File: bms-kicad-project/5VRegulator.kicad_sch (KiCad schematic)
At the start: 22 parts, among them U5 SIC461ED-T1-GE3

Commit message: feat: Forgot to save changes to schematic.
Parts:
- removed C37: 4.7u, FixedWing:CAPC2012X145N, symbol FixedWing:GCM21BC71E475KE36L
- removed R?: 3.3, FixedWing:RESC1608X55N, symbol FixedWing:RK73H1JTTD3R30F
- added R4, R?: 100k, FixedWing:RESC2012X60N, symbol FixedWing:RC0805FR-07100KL
- added R5: 3.3, FixedWing:RESC1608X55N, symbol FixedWing:RK73H1JTTD3R30F
- renumbered C38 to C?, C35 to C?, C36 to C?, U5 to U?
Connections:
- net +BATT: now also C?.2; no longer C?.N
- net GND: now also C?.1; no longer C?.2, C?.2, C?.P, R?.1, R?.1, R?.1, R?.2, R?.2
- net at R?.1, U?.3 (EN): now also R?.2; no longer R?.2
- net at U?.5 (PHASE), U?.6 (PHASE__1): now also C32.2
- net at C32.1: now also R5.2
- net at R?.1: no longer U?.24 (FSW)
- net at U?.4 (BOOT): now also R5.1; no longer C32.2
- new net: R4.1, R?.2
- new net: R4.2, R?.1
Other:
- moved on the sheet: R?

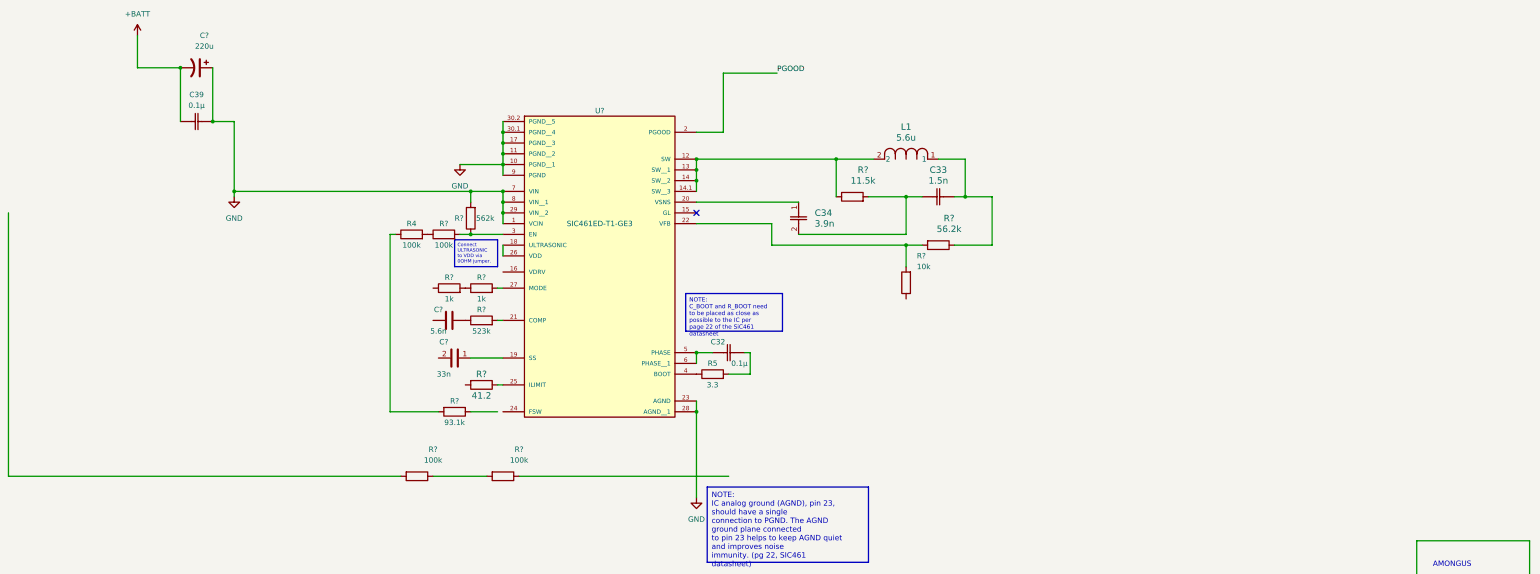
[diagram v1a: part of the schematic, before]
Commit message: feat: Just about completed 5V Regulator Schematic.
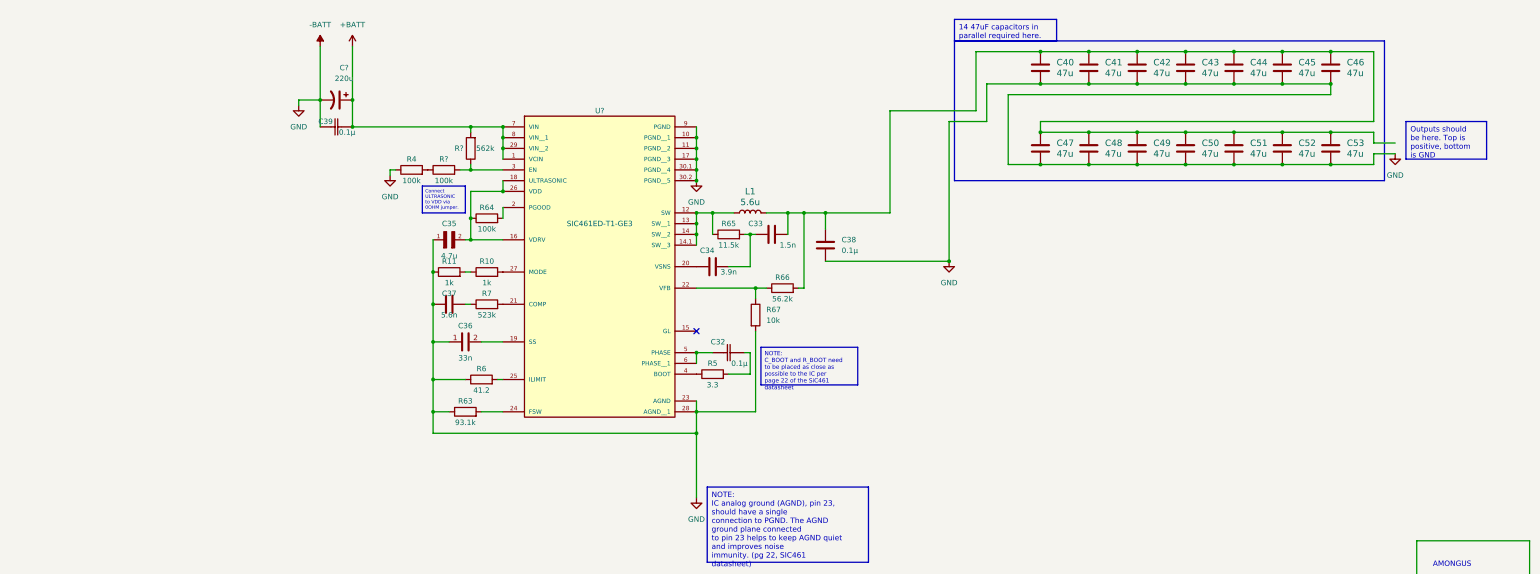
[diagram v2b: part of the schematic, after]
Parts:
- removed C?: 5.6n, FixedWing:G-21_MUR, symbol FixedWing:GRM2195C1H562JA01D
- removed C?: 33n, FixedWing:CAPC2012X94N, symbol FixedWing:08053C333KAT2A
- removed R?: 523k, FixedWing:RC0805N_YAG, symbol FixedWing:RC0805FR-07523KL
- removed R?: 56.2k, FixedWing:RC0805N_YAG, symbol FixedWing:RC0805FR-0756K2L
- removed R?: 41.2, FixedWing:RC0805N_VIS, symbol FixedWing:CRCW080541K2FKEA
- removed R?: 93.1k, FixedWing:RESC2012X60N, symbol FixedWing:RC0805FR-0793K1L
- removed R? (x2): 100k, FixedWing:RESC2012X60N, symbol FixedWing:RC0805FR-07100KL
- removed R?: 10k, FixedWing:KOA_Speer-RK73H2A-0-0-MFG, symbol FixedWing:RK73H2ATTD1002F
- removed R? (x2): 1k, FixedWing:RC0805N_YAG, symbol FixedWing:RC0805FR-071KL
- removed R?: 11.5k, FixedWing:RC0805N_YAG, symbol FixedWing:RC0805FR-0711K5L
- added C35: 4.7u, FixedWing:CAPC2012X145N, symbol FixedWing:GCM21BC71E475KE36L
- added C36: 33n, FixedWing:CAPC2012X94N, symbol FixedWing:08053C333KAT2A
- added C37: 5.6n, FixedWing:G-21_MUR, symbol FixedWing:GRM2195C1H562JA01D
- added C38: 0.1µ, FixedWing:CAP_GCJ-18_MUR, symbol FixedWing:GCJ188R72A104KA01D
- added C40, C41, C42, C43, C44, C45, C46, C47, C48, C49, C50, C51, C52, C53: 47u, FixedWing:G-32_MUR, symbol FixedWing:GRM32ER71A476KE15L
- added R10, R11: 1k, FixedWing:RC0805N_YAG, symbol FixedWing:RC0805FR-071KL
- added R6: 41.2, FixedWing:RC0805N_VIS, symbol FixedWing:CRCW080541K2FKEA
- added R63: 93.1k, FixedWing:RES_ERJ6ENF9312V, symbol FixedWing:ERJ6ENF9312V
- added R64: 100k, FixedWing:RESC2012X60N, symbol FixedWing:RC0805FR-07100KL
- added R65: 11.5k, FixedWing:RC0805N_YAG, symbol FixedWing:RC0805FR-0711K5L
- added R66: 56.2k, FixedWing:RC0805N_YAG, symbol FixedWing:RC0805FR-0756K2L
- added R67: 10k, FixedWing:KOA_Speer-RK73H2A-0-0-MFG, symbol FixedWing:RK73H2ATTD1002F
- added R7: 523k, FixedWing:RC0805N_YAG, symbol FixedWing:RC0805FR-07523KL
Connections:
- net +BATT: now also C39.1, C?.1, R?.2, U?.1 (VCIN), U?.29 (VIN__2), U?.7 (VIN), U?.8 (VIN__1); no longer C39.2, C?.2
- net at U?.21 (COMP): now also R7.2
- net at C33.1, C34.2: now also R65.2
- net at U?.22 (VFB): now also R66.1, R67.2
- net at L1.1: now also U?.12 (SW), U?.13 (SW__1), U?.14 (SW__2), U?.14.1 (SW__3), R65.1; no longer C33.2
- net at U?.25 (ILIMIT): now also R6.2
- net -BATT: now reaches R4.1
- net -BATT: now also C39.2, C?.2, U?.10 (PGND__1), U?.11 (PGND__2), U?.17 (PGND__3), U?.23 (AGND), U?.28 (AGND__1), U?.30.1 (PGND__4), U?.30.2 (PGND__5), U?.9 (PGND), C35.1, C36.1, C37.1, C38.1, C40.1, C41.1, C42.1, C43.1, C44.1, C45.1, C46.1, C47.1, C48.1, C49.1, C50.1, C51.1, C52.1, C53.1, R11.1, R6.1, R63.1, R67.1
- net at U?.16 (VDRV): now also U?.18 (ULTRASONIC), U?.26 (VDD), C35.2, R64.1
- net at U?.19 (SS): now also C36.2
- net at U?.24 (FSW): now also R63.2
- net at U?.27 (MODE): now also R10.2
- removed net GND: C39.1, C?.1, R?.2, U?.1 (VCIN), U?.10 (PGND__1), U?.11 (PGND__2), U?.17 (PGND__3), U?.23 (AGND), U?.28 (AGND__1), U?.29 (VIN__2), U?.30.1 (PGND__4), U?.30.2 (PGND__5), U?.7 (VIN), U?.8 (VIN__1), U?.9 (PGND)
- net PGOOD: no longer names the net of U?.2 (PGOOD)
- net PGOOD: now also R64.2
- new net: C33.2, C38.2, C40.2, C41.2, C42.2, C43.2, C44.2, C45.2, C46.2, C47.2, C48.2, C49.2, C50.2, C51.2, C52.2, C53.2, L1.2, R66.2
- new net: C37.2, R7.1
- new net: R10.1, R11.2
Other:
- moved on the sheet: C39, C?, R4, R?

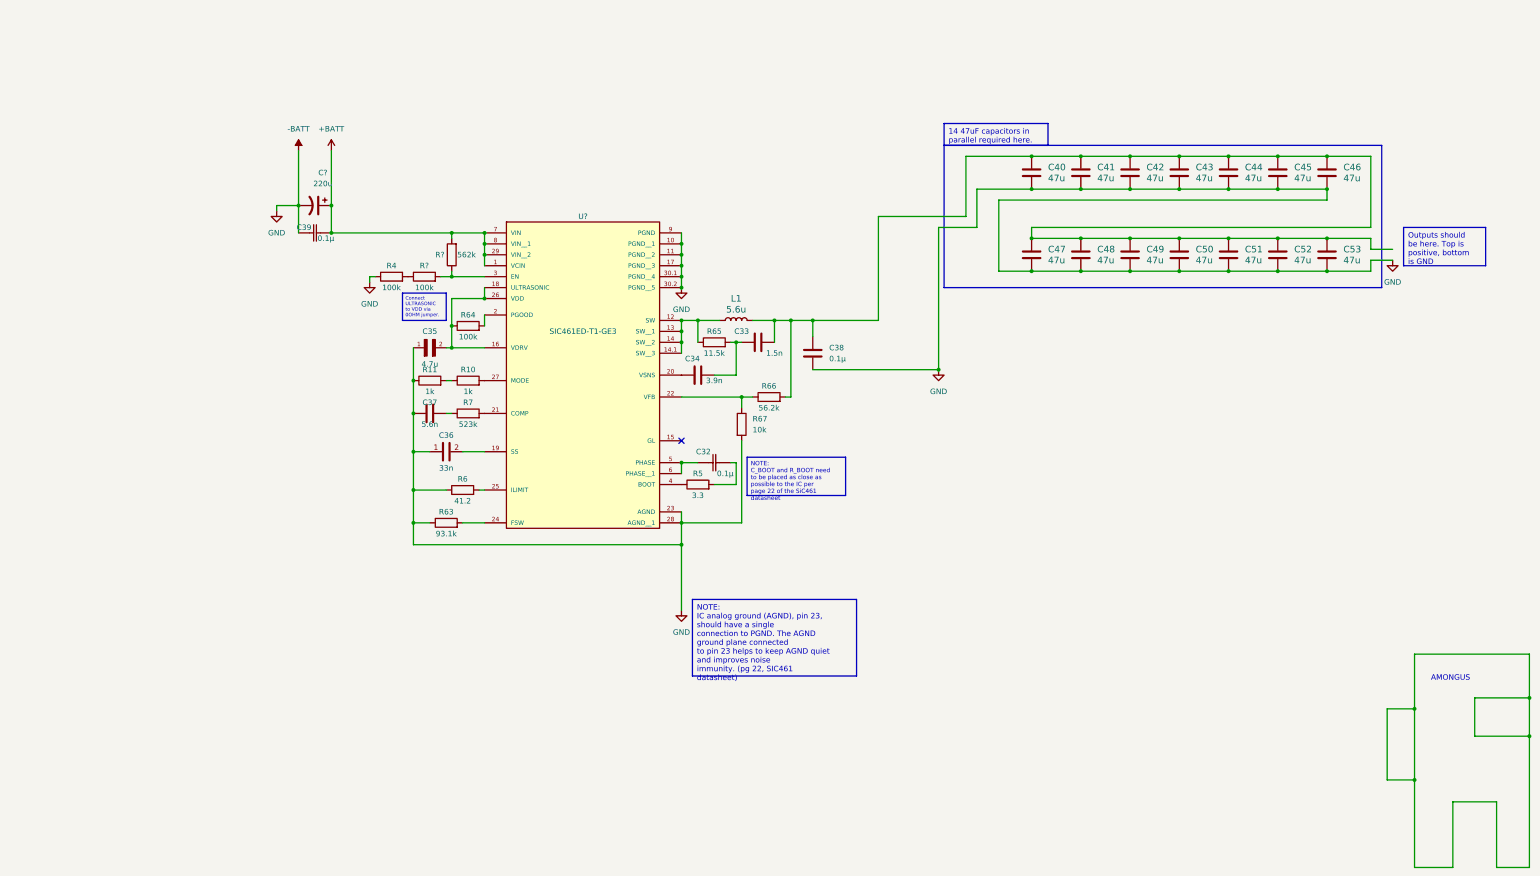
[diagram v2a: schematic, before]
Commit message: feat: cosmetic changes to 5V reg schematic
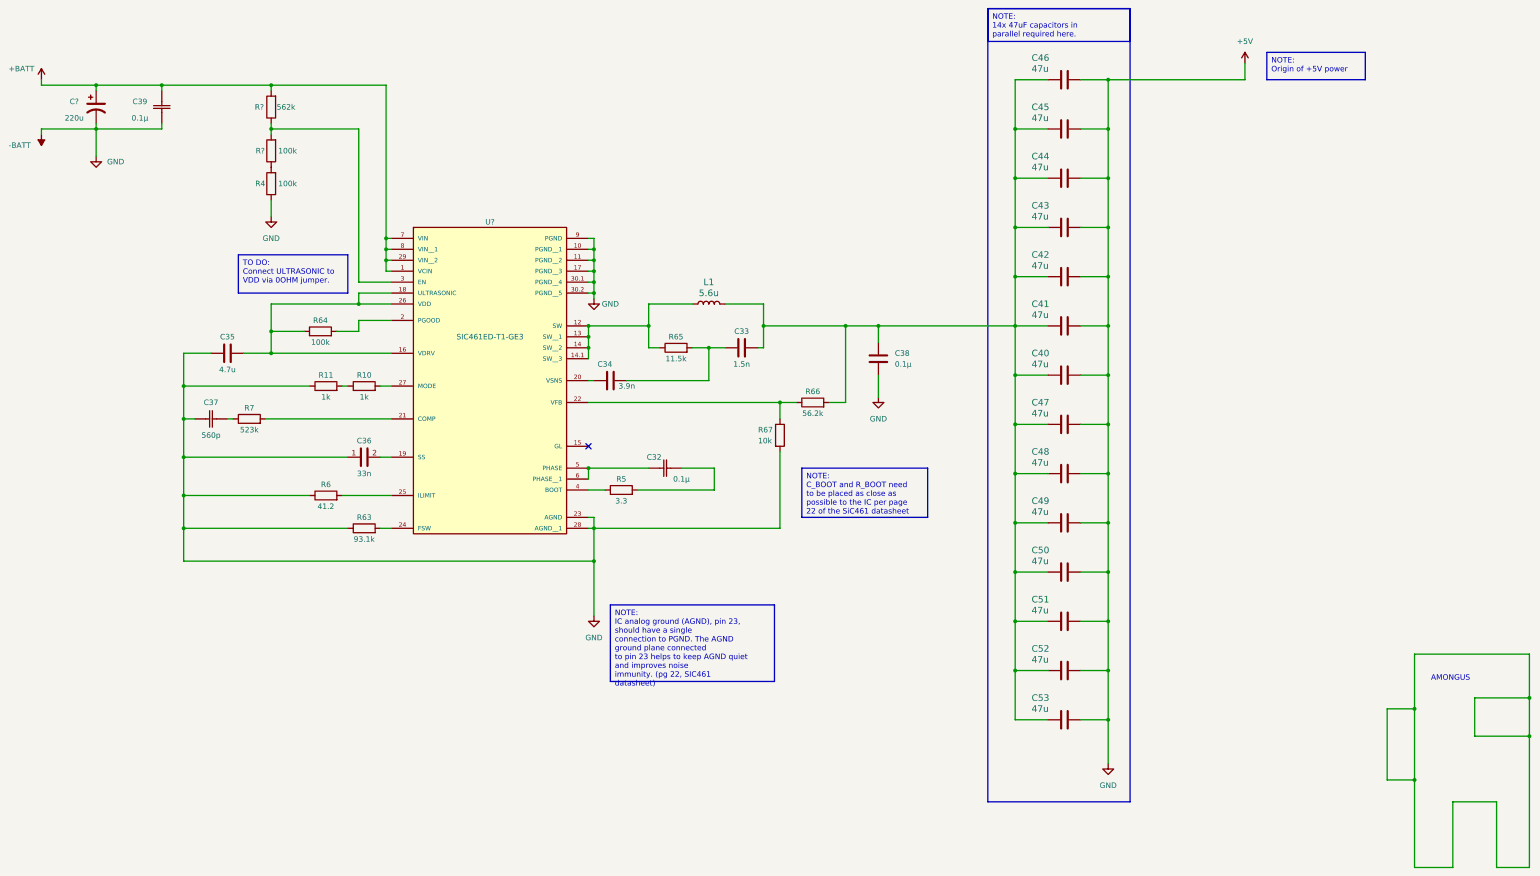
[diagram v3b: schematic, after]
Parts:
- removed C37: 5.6n, FixedWing:G-21_MUR, symbol FixedWing:GRM2195C1H562JA01D
- added C37: 560p, FixedWing:CAP_CC0805_YAG, symbol FixedWing:CC0805JRNPO9BN561
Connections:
- net at R7.1: now also C37.2
- net -BATT renamed +5V
- net +5V: now also C37.1
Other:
- moved on the sheet: C32, C33, C34, C36, C38, C39, C40, C41, C42, C43, C44, C45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

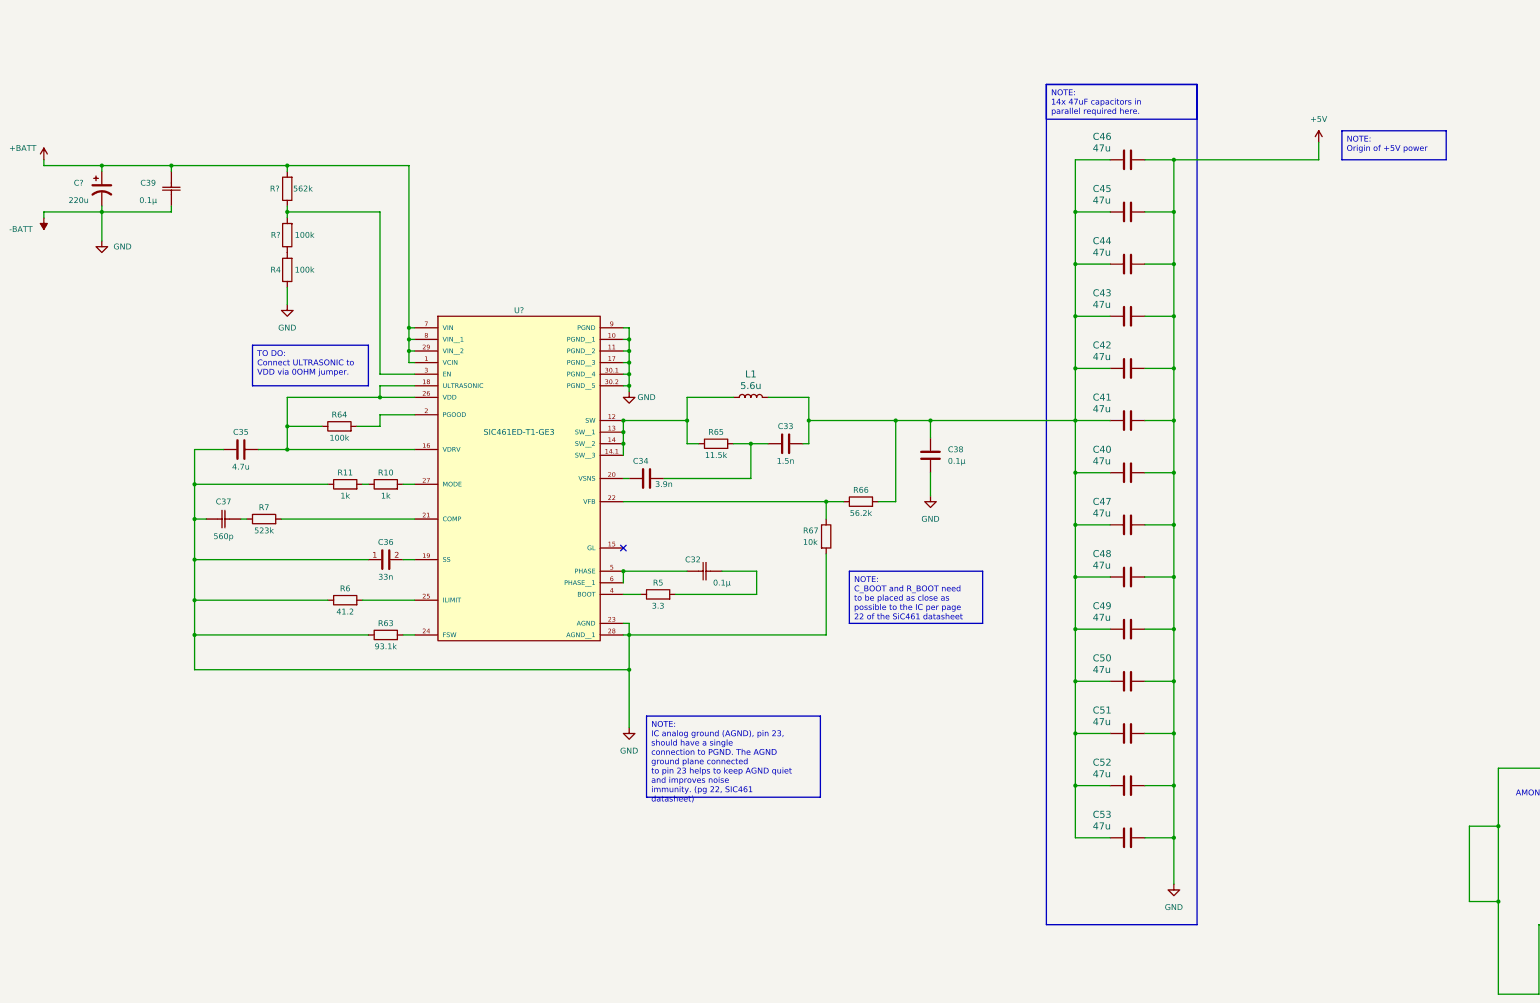
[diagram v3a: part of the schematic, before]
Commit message: feat: Added comment boxes and fixed 5V Regulator Schematic.
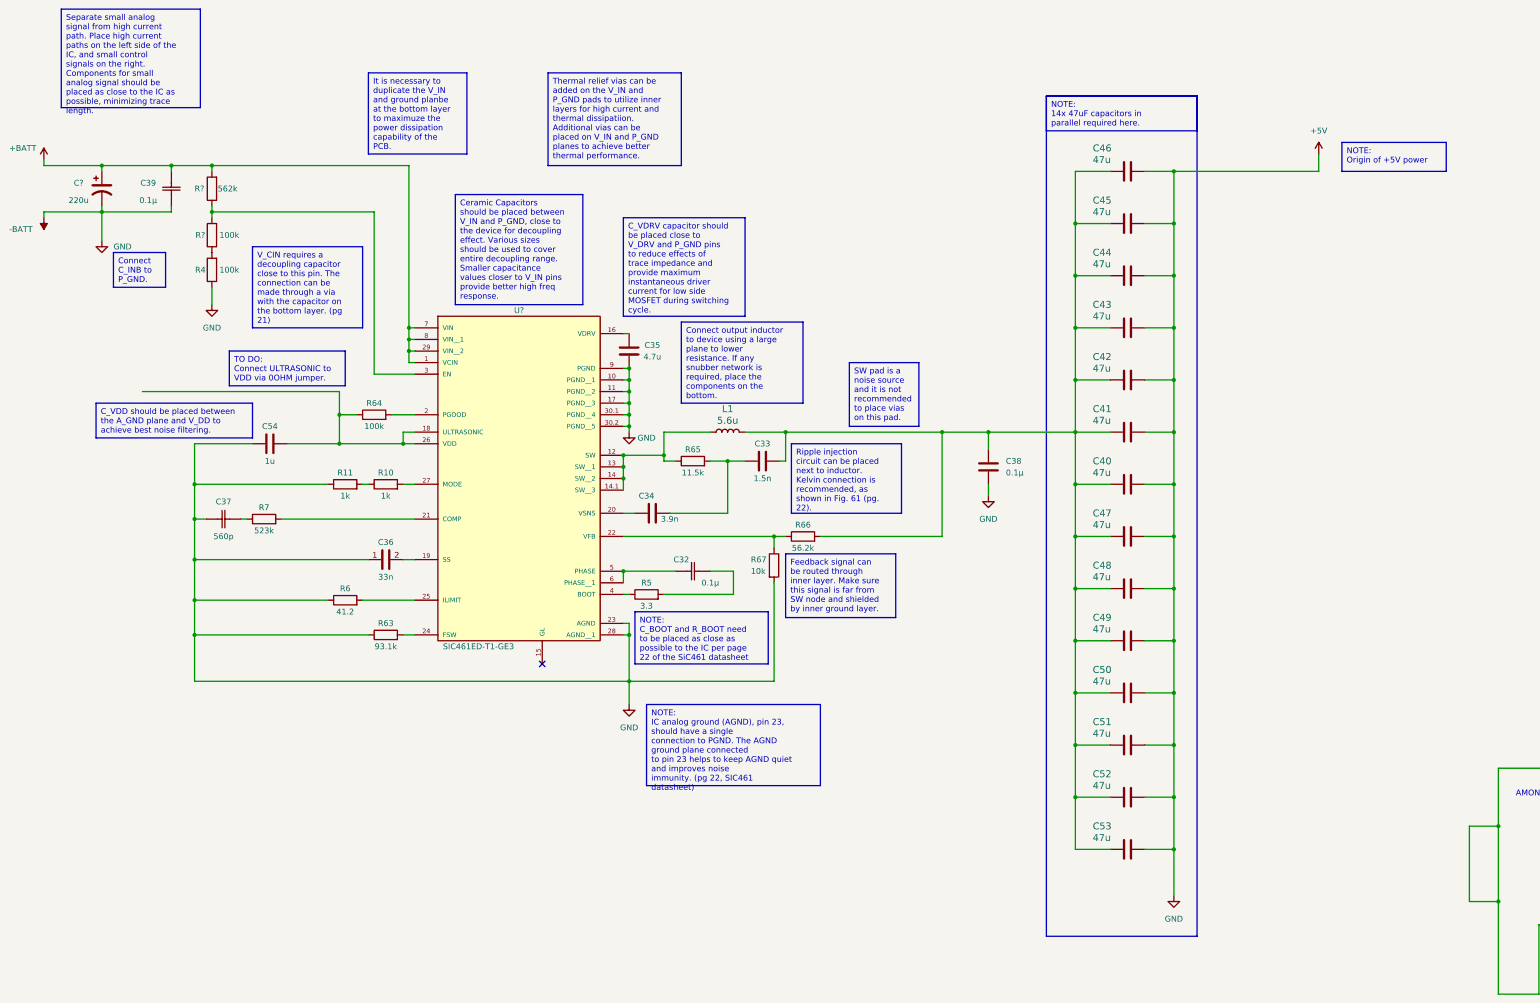
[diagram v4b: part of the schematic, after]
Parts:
- added C54: 1u, FixedWing:CAPC1608X90N, symbol FixedWing:GCM188R71C105KA64D
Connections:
- net +5V: now also C54.2
- net at R64.1, U?.18 (ULTRASONIC), U?.26 (VDD): now also C54.1; no longer C35.2, U?.16 (VDRV)
- new net: C35.2, U?.16 (VDRV)
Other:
- moved on the sheet: C32, C33, C34, C35, C38, C40, C41, C42, C43, C44, C45, C46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

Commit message: feat: just moved around and edited notes on the 5V reg schematic
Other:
- note removed: "AMONGUS"
- moved on the sheet: C32, C33, C34, C35, C36, C37, C38, C39, C40, C41, C42, C43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
